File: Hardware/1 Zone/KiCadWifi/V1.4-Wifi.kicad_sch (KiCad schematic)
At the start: 131 parts, among them CN11 Pinheader 1x12 P2.54 Horizont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, CN16 Pinheader 1x02 P2.54 Horizont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, Q1 AOD4184A, Q10 PJA3404A, Q11 PJA3404A, Q12 BC816-16VL, Q8 UMH3NTN, SW1 K2-1102DP-G3SW-04, SW2 K2-1102DP-G3SW-04, SW3 K2-1102DP-G3SW-04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

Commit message: Tidied up schematics
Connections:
- net 3.3V: now also C27.1; no longer C27.2
- net BUZZER: now also R46.2; no longer R46.1
- net GND: now also C27.2, R46.1; no longer C27.1, R46.2
- no-connect marks 38 -> 37
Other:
- moved on the sheet: BUZZER1, C1, C10, C11, C12, C13, C14, C15, C16, C17, C18, C19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

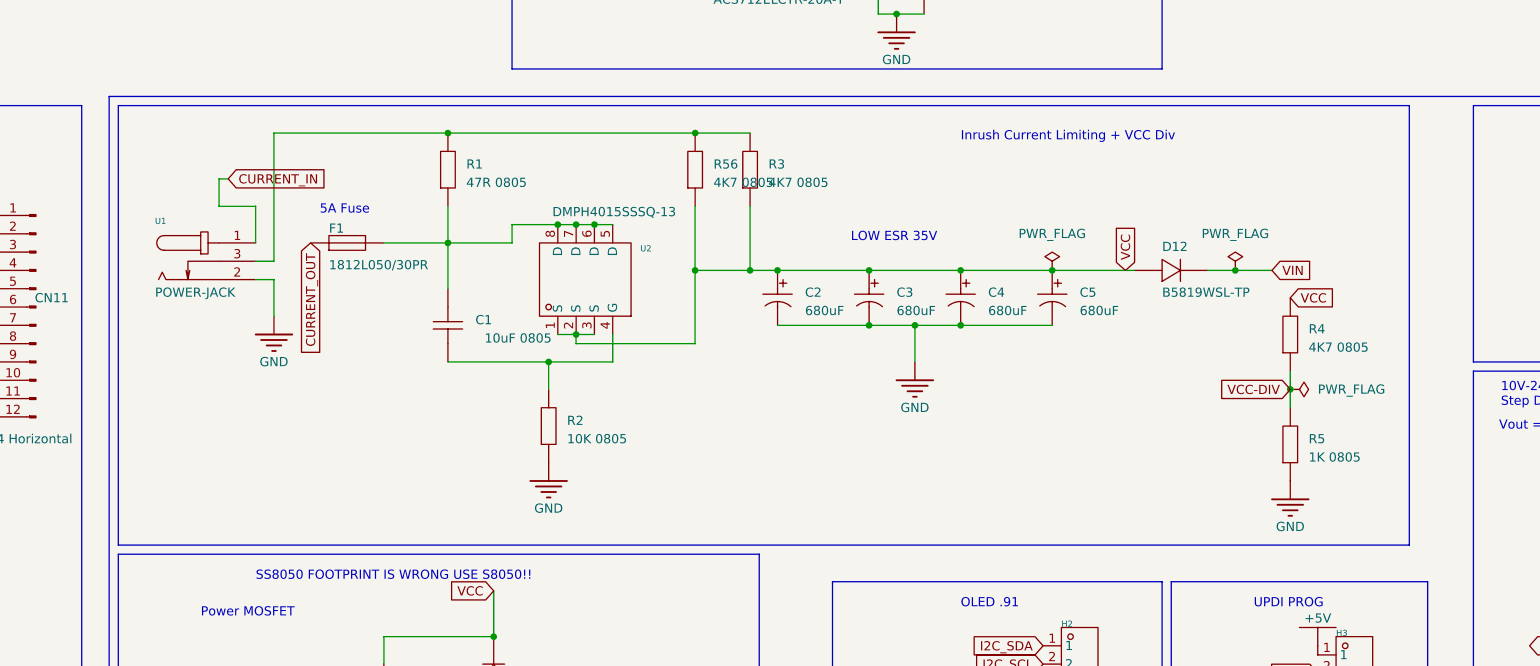
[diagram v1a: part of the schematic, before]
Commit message: Replaced Power Jack with screw terminals. Repurposed R3 to bleeder resistor. R1, R53 removed.
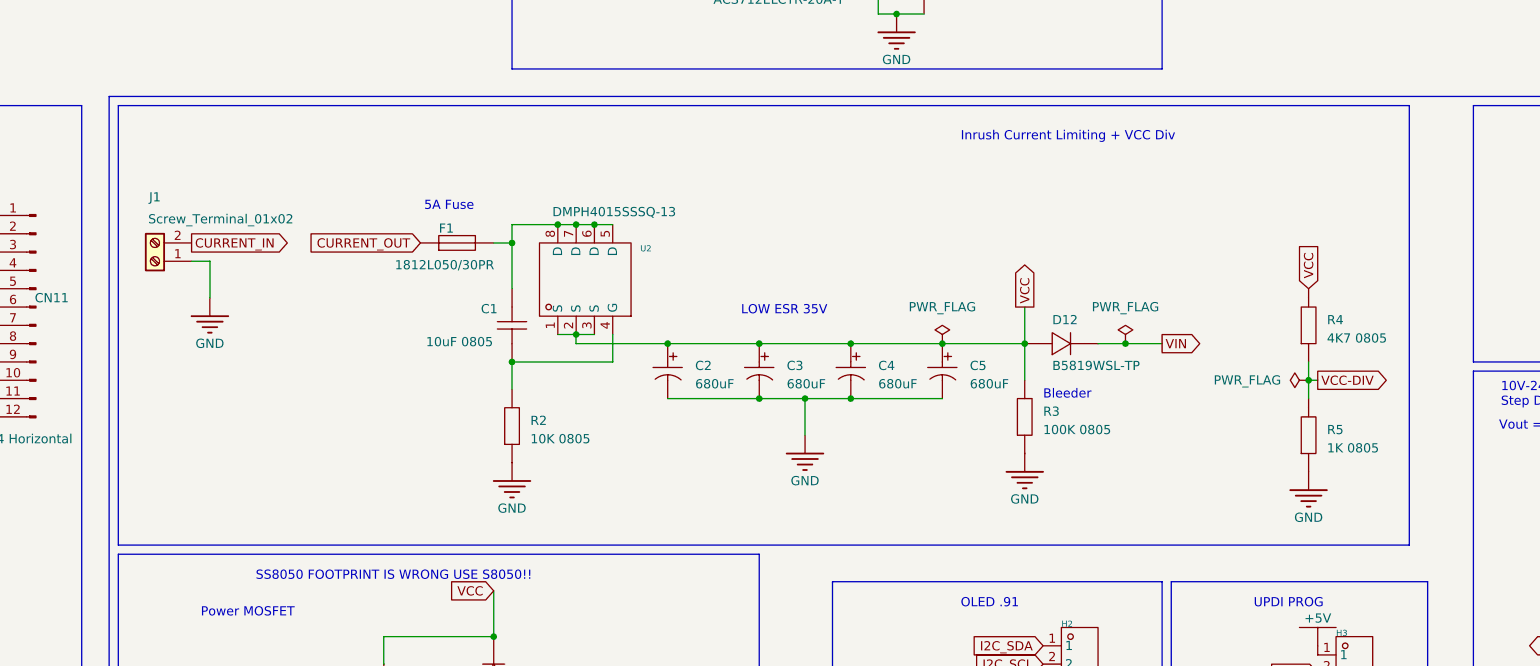
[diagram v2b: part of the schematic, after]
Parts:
- removed R1: 47R 0805, Resistor_SMD:R_0805_2012Metric_Pad1.20x1.40mm_HandSolder, symbol V1.4-Wifi-easyedapro:Res
- removed R56: 4K7 0805, Resistor_SMD:R_0805_2012Metric_Pad1.20x1.40mm_HandSolder, symbol V1.4-Wifi-easyedapro:Res
- removed U1: POWER-JACK, V1.4-Wifi-easyedapro:DC-IN-TH_POWER-JACK, symbol V1.4-Wifi-easyedapro:POWER-JACK
- added J1: Screw_Terminal_01x02, TerminalBlock_Phoenix:TerminalBlock_Phoenix_MKDS-1,5-2_1x02_P5.00mm_Horizontal, symbol Connector:Screw_Terminal_01x02
- R3: value 4K7 0805 -> 100K 0805
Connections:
- net CURRENT_IN: now also J1.2 (Pin_2)
- net GND: now also R3.1, J1.1 (Pin_1)
- net VCC: now also R3.2; no longer R3.1
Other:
- note added: "Bleeder"
- moved on the sheet: C1, C2, C3, C4, C5, D12, F1, R2, R4, R5

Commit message: Rerouting for tighter return paths for MOSI and SCK. Moved R4,R5 to avoid cutting return path. Renamed LCD_RST, CD, DC to TFT_RST, TFT_CS, TFT_CS to better align with code.
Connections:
- net CS renamed TFT_CS
- net DC renamed TFT_DC
- net LCD_CS_OUT renamed TFT_CS_OUT
- net LCD_DC_OUT renamed TFT_DC_OUT
- net LCD_RST renamed TFT_RST
- net LCD_RST_OUT renamed TFT_RST_OUT

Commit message: Removed H10 7pin header for TFT, for EMC reasons.
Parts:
- removed H10: Female 1x07 P2.54 vertical tall, V1.4-Wifi-easyedapro:HDR-TH_7P-P2.54-V-F, symbol V1.4-Wifi-easyedapro:220S-1*7P H=8.5MM Ytype Gold-plated
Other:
- note added: "TFT Connector 7Pin (removed for EMC reasons)"
- note removed: "TFT Connector 7Pin"

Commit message: Renamed TFT_LED, TFT_SI_OUT, TFT_SCK_OUT to LCD_* for consistency
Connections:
- net LCD_LED renamed TFT_LED
- net LCD_SCK_OUT renamed TFT_SCK_OUT
- net LCD_SI_OUT renamed TFT_SI_OUT

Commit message: Moved D8 for EMC reasons. Refactored Fan ctrl schematic. BOM details corrected.
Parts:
- C2, C3, C4, C5: Manufacturer Rubycon -> Panasonic; mpn 35ZLH680MEFC10X23 -> EEU-FR1V681B
- H11, H12: value A2541HWR-2x6P -> 68021-412HLF; Manufacturer CJT(长江连接器) -> Amphenol; mpn A2541HWR-2x6P -> 68021-412HLF
- H15: value A2541HWR-2x4P -> 68021-208HLF; Manufacturer CJT(长江连接器) -> Amphenol
- J1: mpn (none) -> 68021-208HLF
- LED10: mpn LTST-C150KRKT -> LTST-C250KRKT
- Q1: value AOD4184A -> IPD90N04S403ATMA1
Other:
- note removed: "Changed mosfet to AOD4184A Old one kept shorting"
- moved on the sheet: CN16, D8, Q11, R40, R47, R48, U17

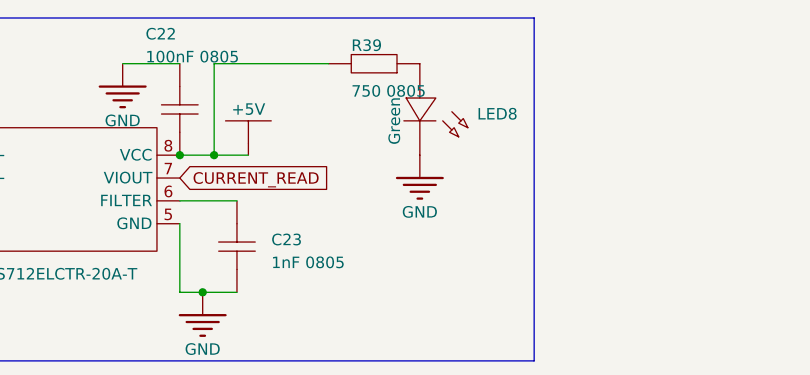
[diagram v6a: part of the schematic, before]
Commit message: BOM detailes corrected
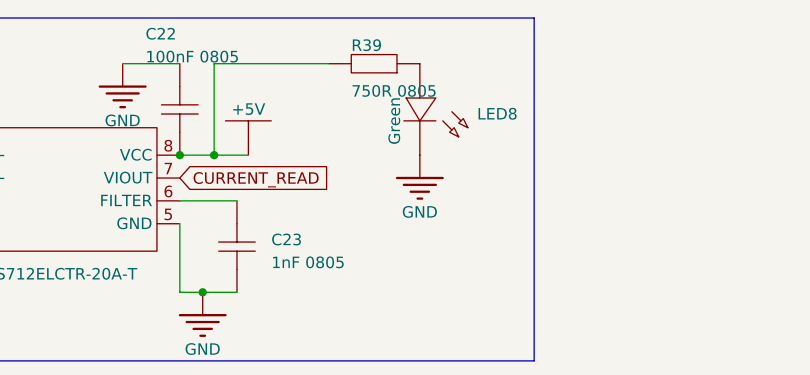
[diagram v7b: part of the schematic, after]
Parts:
- R39: value 750 0805 -> 750R 0805
- R6: Manufacturer (none) -> Susumu; mpn (none) -> KRL1220E-M-R330-F

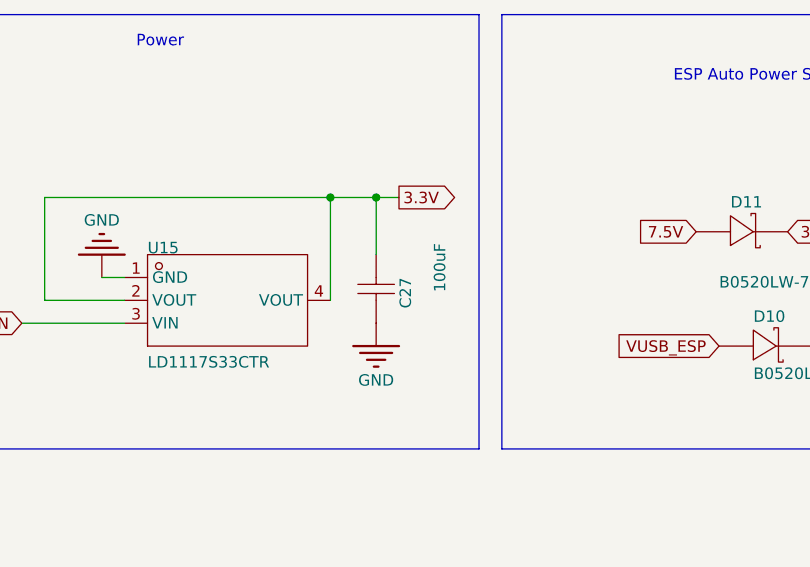
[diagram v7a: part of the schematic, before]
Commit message: Changed C27 to T491B107M010AT due to availablility
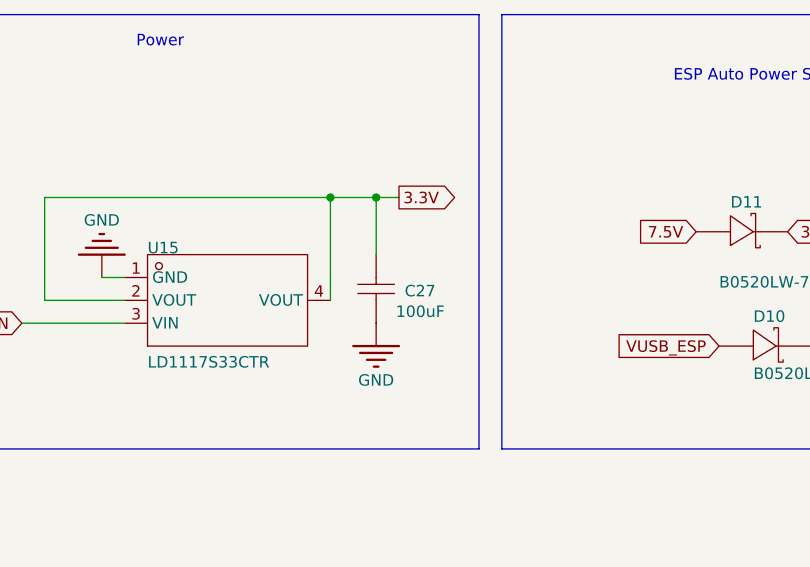
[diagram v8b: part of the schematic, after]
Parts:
- C27: footprint V1.4-Wifi-easyedapro:C1206 -> V1.4-Wifi-easyedapro:CAP-SMD_L3.5-W2.8-R-RD; Manufacturer SAMSUNG -> KEMET; mpn CL31A107MQHNNNE -> T491B107M010AT
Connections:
- net 3.3V: now also C27.2; no longer C27.1
- net GND: now also C27.1; no longer C27.2
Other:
- moved on the sheet: C27
